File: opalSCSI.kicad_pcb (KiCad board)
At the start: 2 copper layers, 53.8 x 42.2 mm, 75 parts, among them J1 Amphenol L717SDB25PA4CH3R, J2 PGM, J3 Micro_SD_Card, J4 USB_B_Micro, SW1 RST, U1 STM32F103CBTx, U2 LT1117-3.3, Y1 8Mhz, Y2 CM7V-T1A-32.768k-9pF-20PPM-TA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

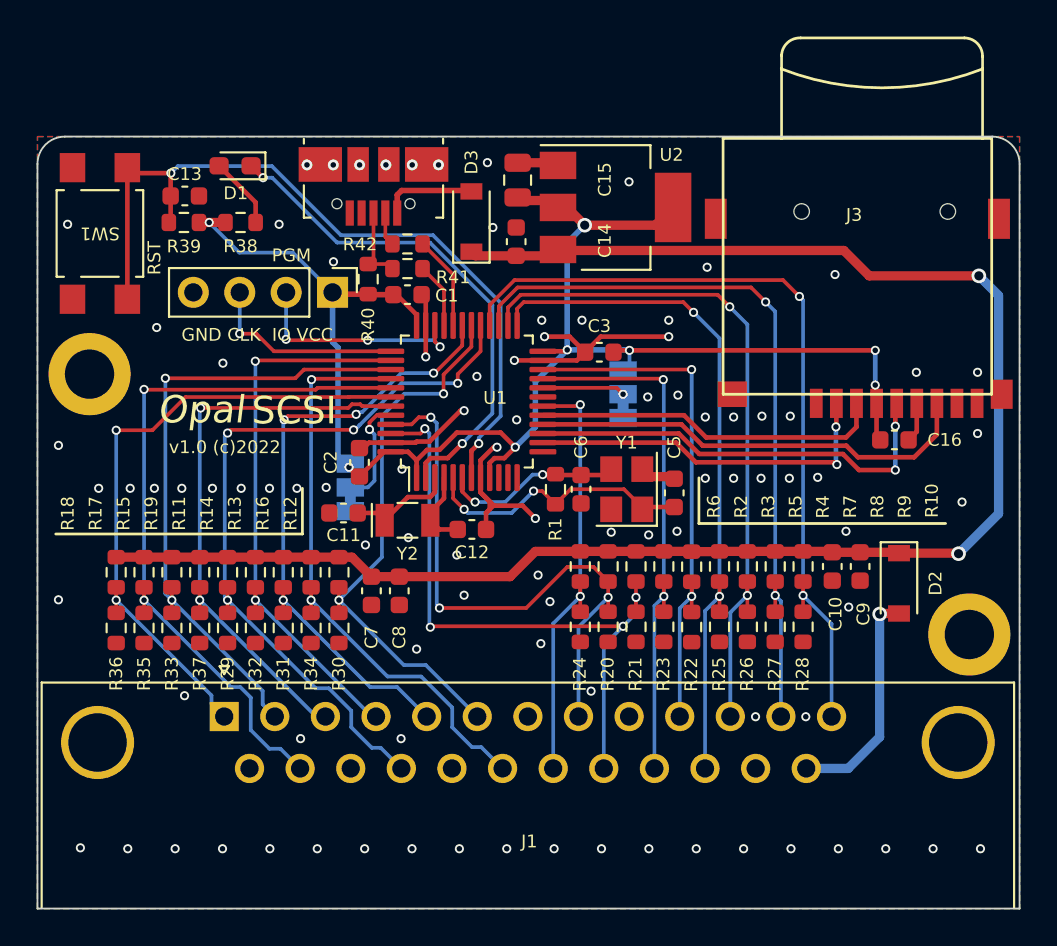
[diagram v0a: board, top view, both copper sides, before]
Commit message: Add nReset pin to programming (SWD) header
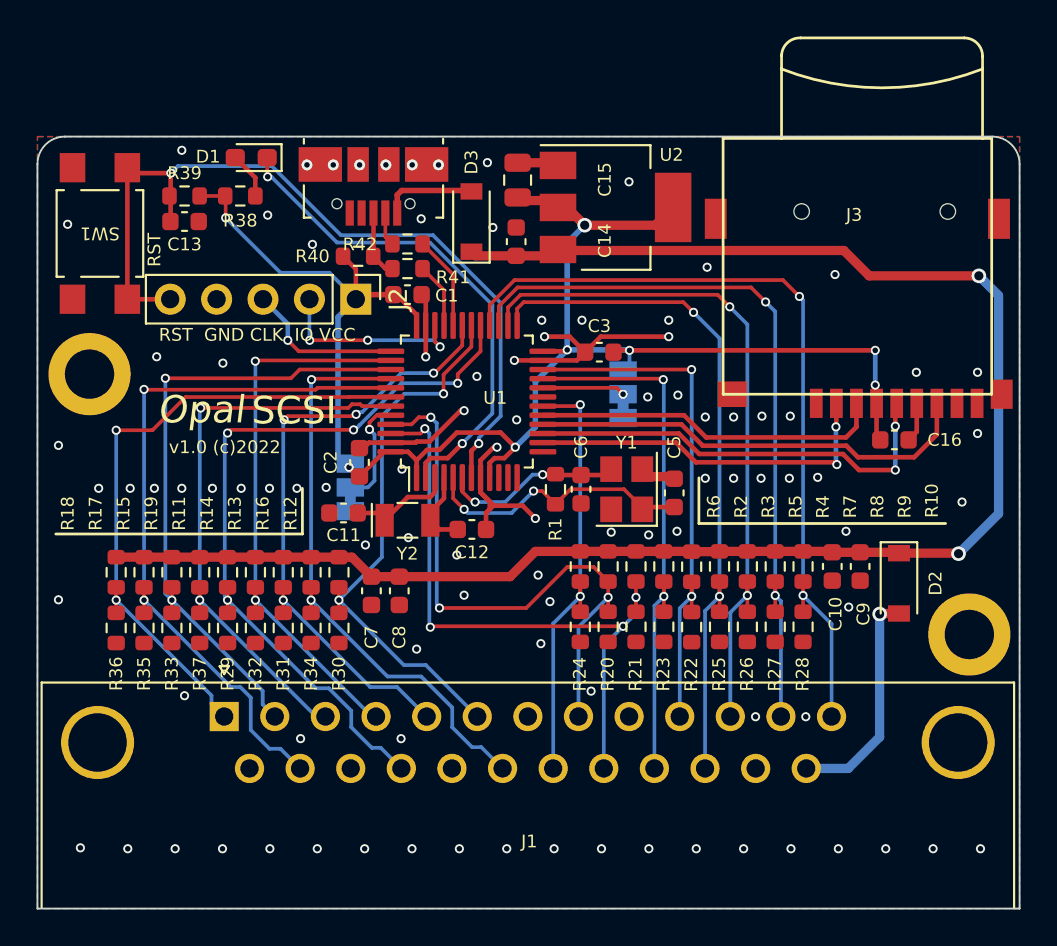
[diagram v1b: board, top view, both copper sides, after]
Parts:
- J2: footprint Connector_PinHeader_2.54mm:PinHeader_1x04_P2.54mm_Vertical -> Connector_PinHeader_2.54mm:PinHeader_1x05_P2.54mm_Vertical
- moved R39 1.45 mm to (86.8, 64.8)
- moved R38 1.45 mm to (89.8, 64.8)
- moved C13 1.40 mm to (86.8, 66.2)
- moved R40 1.37 mm to (96.3, 68.0), turned to 0 degrees
- moved J2 1.33 mm to (96.2, 70.4)
- moved D1 0.99 mm to (90.5, 62.6)
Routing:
- net VCC: track 88.7 -> 91.8 mm
- net /SWD_CLK: track 10.9 -> 8.70 mm
- net /~{RESET}: track 44.0 -> 46.2 mm
- net /SWD_IO: track 12.5 -> 10.8 mm
- net Net-(D1-Pad2): track 3.93 -> 2.56 mm
- net Net-(J4-Pad3): track 4.34 -> 3.70 mm
- net GND: vias 94 -> 96
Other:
- board text added: "RST GND CLK IO VCC"
- board text removed: "GND CLK IO VCC"
